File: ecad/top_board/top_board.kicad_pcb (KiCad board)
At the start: 2 copper layers, 107 x 79 mm, 110 parts, among them Q1 RE1C002UN, Q10 RE1C002UN, Q2 RE1C002UN, Q3 RE1C002UN, Q4 RE1C002UN, Q5 RE1C002UN, Q6 RE1C002UN, Q7 RE1C002UN, Q8 RE1C002UN, Q9 RE1C002UN, SW1 PEL12T, SW10 PEL12T, SW11 PEL12T, SW12 PEL12T, SW13 PEL12T, SW14 PEL12T, SW15 PEL12T, SW16 SW_Push, SW17 SW_Push, SW18 SW_Push, SW19 SW_Push, SW2 SW_Push, SW20 SW_Push, SW3 PEL12T, SW4 SW_Push, SW5 PEL12T, SW6 SW_Push, SW7 SW_Push, SW8 PEL12T, SW9 SW_Push, U1 TLC5973, U10 TLC5973, U2 TLC5973, U3 TLC5973, U4 TLC5973, U5 TLC5973, U6 TLC5973, U7 TLC5973, U8 TLC5973, U9 TLC5973

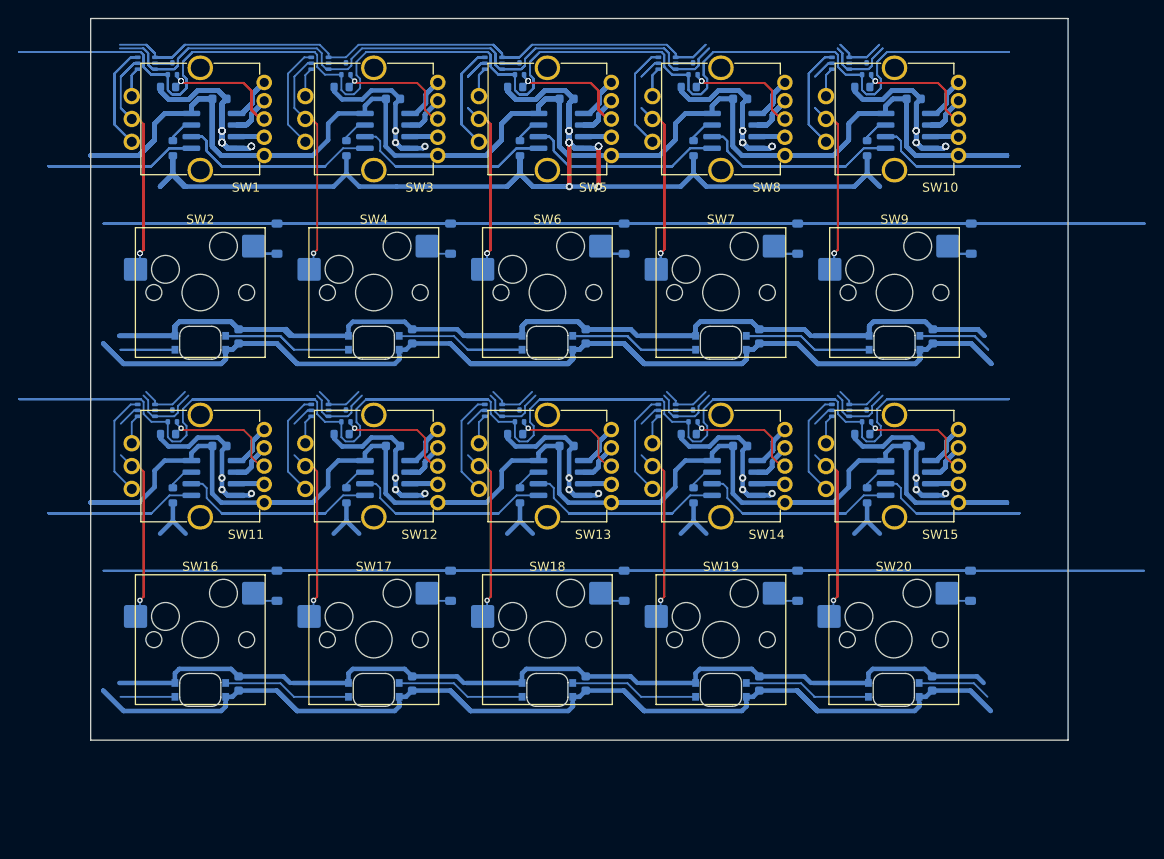
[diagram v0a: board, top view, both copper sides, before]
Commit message: Draft a slightly smaller top board
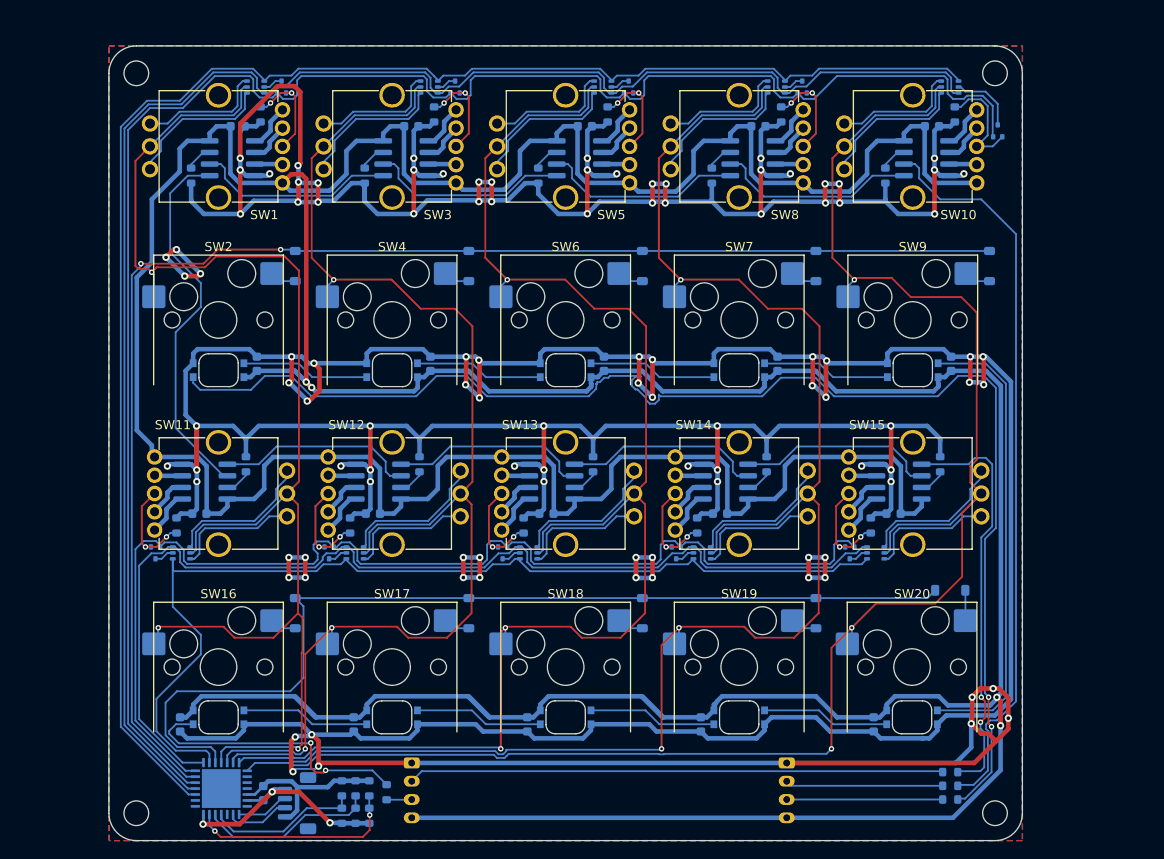
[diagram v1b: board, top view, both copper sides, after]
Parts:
- added C21: 100n, Capacitor_SMD:C_0603_1608Metric, B.Cu at (66.9, 133.8)
- added J1: JST PH, Connector_JST:JST_PH_S4B-PH-K_1x04_P2.00mm_Horizontal, B.Cu at (124.2, 130.5)
- added J2: JST PH, Connector_JST:JST_PH_S4B-PH-K_1x04_P2.00mm_Horizontal, B.Cu at (83.2, 130.5)
- added J3: JST SH, Connector_JST:JST_SH_BM04B-SRSS-TB_1x04-1MP_P1.00mm_Vertical, B.Cu at (70.6, 134.9)
- added R21: 11k, Resistor_SMD:R_0603_1608Metric, B.Cu at (77.0, 133.3)
- added R22: 11k, Resistor_SMD:R_0603_1608Metric, B.Cu at (75.5, 133.3)
- added R23: 11k, Resistor_SMD:R_0603_1608Metric, B.Cu at (78.5, 133.3)
- added R24: 11k, Resistor_SMD:R_0603_1608Metric, B.Cu at (78.5, 136.3)
- added R25: 11k, Resistor_SMD:R_0603_1608Metric, B.Cu at (77.0, 136.3)
- added R26: 11k, Resistor_SMD:R_0603_1608Metric, B.Cu at (75.5, 136.3)
- added R27: 33, Resistor_SMD:R_0603_1608Metric, B.Cu at (80.4, 133.7)
- added R28: 33, Resistor_SMD:R_0603_1608Metric, B.Cu at (142.1, 134.5)
- added R29: 33, Resistor_SMD:R_0603_1608Metric, B.Cu at (142.1, 133.0)
- added R30: 33, Resistor_SMD:R_0603_1608Metric, B.Cu at (142.1, 131.5)
- added REF**: MountingHole_2.7mm_M2.5, MountingHole:MountingHole_2.7mm_M2.5, F.Cu at (53.0, 55.0)
- added REF**: MountingHole_2.7mm_M2.5, MountingHole:MountingHole_2.7mm_M2.5, F.Cu at (147.0, 136.0)
- added REF**: MountingHole_2.7mm_M2.5, MountingHole:MountingHole_2.7mm_M2.5, F.Cu at (147.0, 55.0)
- added REF**: MountingHole_2.7mm_M2.5, MountingHole:MountingHole_2.7mm_M2.5, F.Cu at (53.0, 136.0)
- added U11: MCP23017_ML, Package_DFN_QFN:QFN-28-1EP_6x6mm_P0.65mm_EP4.25x4.25mm, B.Cu at (62.3, 133.3)
- moved D20 16.1 mm to (133.9, 107.5), turned to 180 degrees
- moved D16 16.1 mm to (57.9, 107.5), turned to 180 degrees
- moved D17 16.1 mm to (76.9, 107.5), turned to 180 degrees
- moved D18 16.1 mm to (95.9, 107.5), turned to 180 degrees
- moved D19 16.1 mm to (114.9, 107.5), turned to 180 degrees
- moved Q5 15.9 mm to (147.3, 61.3)
- moved Q10 15.1 mm to (131.1, 107.5), turned to -90 degrees
- moved Q6 15.1 mm to (55.1, 107.5), turned to -90 degrees
- moved Q7 15.1 mm to (74.1, 107.5), turned to -90 degrees
- moved Q8 15.1 mm to (93.1, 107.5), turned to -90 degrees
- moved Q9 15.1 mm to (112.1, 107.5), turned to -90 degrees
- moved D1 12.2 mm to (66.1, 56.5)
- moved D12 12.2 mm to (123.1, 56.5)
- moved D4 12.2 mm to (85.1, 56.5)
- moved D7 12.2 mm to (104.1, 56.5)
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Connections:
- D1 pad 1: /RotaryEncoder_COL1/H_QA -> /RotaryEncoder_COL1/H_QB
- D1 pad 3: /RotaryEncoder_COL1/H_QB -> /RotaryEncoder_COL1/H_QA
- D1 pad 4: /R1_QB -> /R1_QA
- D1 pad 6: /R1_QA -> /R1_QB
- D12 pad 1: /RotaryEncoder_COL4/H_QA -> /RotaryEncoder_COL4/H_QB
- D12 pad 3: /RotaryEncoder_COL4/H_QB -> /RotaryEncoder_COL4/H_QA
- D12 pad 4: /R1_QB -> /R1_QA
- D12 pad 6: /R1_QA -> /R1_QB
- D13 pad 2: /KeyboardKey_COL5/DOUT -> /KeyboardKey_COL10/DIN
- D15 pad 1: /RotaryEncoder_COL5/H_QA -> /RotaryEncoder_COL5/H_QB
- D15 pad 3: /RotaryEncoder_COL5/H_QB -> /RotaryEncoder_COL5/H_QA
- D15 pad 4: /R1_QB -> /R1_QA
- D15 pad 6: /R1_QA -> /R1_QB
- D16 pad 1: /RotaryEncoder_COL6/H_QA -> /RotaryEncoder_COL6/H_QB
- D16 pad 3: /RotaryEncoder_COL6/H_QB -> /RotaryEncoder_COL6/H_QA
- D16 pad 4: /R3_QB -> /R3_QA
- D16 pad 6: /R3_QA -> /R3_QB
- D17 pad 1: /RotaryEncoder_COL7/H_QA -> /RotaryEncoder_COL7/H_QB
- D17 pad 3: /RotaryEncoder_COL7/H_QB -> /RotaryEncoder_COL7/H_QA
- D17 pad 4: /R3_QB -> /R3_QA
- D17 pad 6: /R3_QA -> /R3_QB
- D18 pad 1: /RotaryEncoder_COL8/H_QA -> /RotaryEncoder_COL8/H_QB
- D18 pad 3: /RotaryEncoder_COL8/H_QB -> /RotaryEncoder_COL8/H_QA
- D18 pad 4: /R3_QB -> /R3_QA
- D18 pad 6: /R3_QA -> /R3_QB
- D19 pad 1: /RotaryEncoder_COL9/H_QA -> /RotaryEncoder_COL9/H_QB
- D19 pad 3: /RotaryEncoder_COL9/H_QB -> /RotaryEncoder_COL9/H_QA
- D19 pad 4: /R3_QB -> /R3_QA
- D19 pad 6: /R3_QA -> /R3_QB
- D20 pad 1: /RotaryEncoder_COL10/H_QA -> /RotaryEncoder_COL10/H_QB
- D20 pad 3: /RotaryEncoder_COL10/H_QB -> /RotaryEncoder_COL10/H_QA
- D20 pad 4: /R3_QB -> /R3_QA
- D20 pad 6: /R3_QA -> /R3_QB
- D23 pad 2: /KeyboardKey_COL7/DOUT -> /KeyboardKey_COL6/DIN
- D23 pad 4: /KeyboardKey_COL6/DOUT -> /KeyboardKey_COL7/DIN
- D25 pad 2: /KeyboardKey_COL8/DOUT -> /KeyboardKey_COL7/DIN
- D25 pad 4: /KeyboardKey_COL7/DOUT -> /KeyboardKey_COL8/DIN
- D27 pad 2: /KeyboardKey_COL10/DIN -> /KeyboardKey_COL8/DIN
- D27 pad 4: /KeyboardKey_COL8/DOUT -> /KeyboardKey_COL10/DOUT
- D4 pad 1: /RotaryEncoder_COL2/H_QA -> /RotaryEncoder_COL2/H_QB
- D4 pad 3: /RotaryEncoder_COL2/H_QB -> /RotaryEncoder_COL2/H_QA
- D4 pad 4: /R1_QB -> /R1_QA
- D4 pad 6: /R1_QA -> /R1_QB
- D7 pad 1: /RotaryEncoder_COL3/H_QA -> /RotaryEncoder_COL3/H_QB
- D7 pad 3: /RotaryEncoder_COL3/H_QB -> /RotaryEncoder_COL3/H_QA
- D7 pad 4: /R1_QB -> /R1_QA
- D7 pad 6: /R1_QA -> /R1_QB
- SW19 pad 1: /KeyboardKey_COL9/COL -> /COL4
- U6 pad 6: /RotaryEncoder_COL6/SDI -> /RotaryEncoder_COL1/SDO
- U7 pad 5: /RotaryEncoder_COL6/SDI -> /RotaryEncoder_COL7/SDO
- U7 pad 6: /RotaryEncoder_COL7/SDI -> /RotaryEncoder_COL6/SDO
- U8 pad 5: /RotaryEncoder_COL7/SDI -> /RotaryEncoder_COL8/SDO
- U8 pad 6: /RotaryEncoder_COL8/SDI -> /RotaryEncoder_COL7/SDO
- U9 pad 5: /RotaryEncoder_COL8/SDI -> /RotaryEncoder_COL10/SDI
- U9 pad 6: /RotaryEncoder_COL10/SDO -> /RotaryEncoder_COL8/SDO
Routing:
- net /R1_SW: track 1670.6 -> 193.9 mm
- net +5V: track 1909.9 -> 646.4 mm, vias 0 -> 4
- net /R3_SW: track 1133.4 -> 124.1 mm
- net /R2_SW: track 494.0 -> 153.4 mm, vias 0 -> 2
- net /RotaryEncoder_COL3/SDI: track 341.7 -> 22.1 mm
- net /R4_SW: track 380.0 -> 106.7 mm
- net /RotaryEncoder_COL4/SDI: track 291.9 -> 22.1 mm
- net /RotaryEncoder_COL6/SDI: track 191.1 -> 0.00 mm
- net /RotaryEncoder_COL7/SDI: track 191.1 -> 0.00 mm
- net /RotaryEncoder_COL8/SDI: track 191.1 -> 0.00 mm
- net /RotaryEncoder_COL1/SDI: track 212.4 -> 22.0 mm
- net /RotaryEncoder_COL2/SDI: track 211.9 -> 21.9 mm
- net /RotaryEncoder_COL1/SDO: track 195.3 -> 40.8 mm
- net /RotaryEncoder_COL10/SDO: track 191.1 -> 45.6 mm, vias 0 -> 2
- net /KeyboardKey_COL1/DIN: track 11.9 -> 149.1 mm, vias 0 -> 2
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- added copper zone on B.Cu, net GND
- added copper zone on F.Cu, net GND
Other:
- board size 107 x 79 mm -> 100 x 87 mm
